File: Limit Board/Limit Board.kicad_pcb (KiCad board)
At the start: 2 copper layers, 4 parts, among them J1 Conn_01x02_Socket

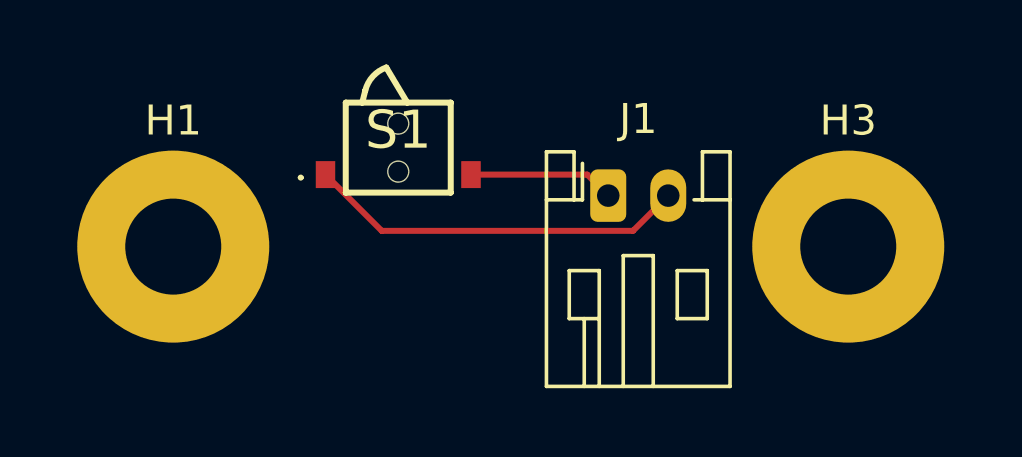
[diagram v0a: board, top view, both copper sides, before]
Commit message: Fix edge cuts
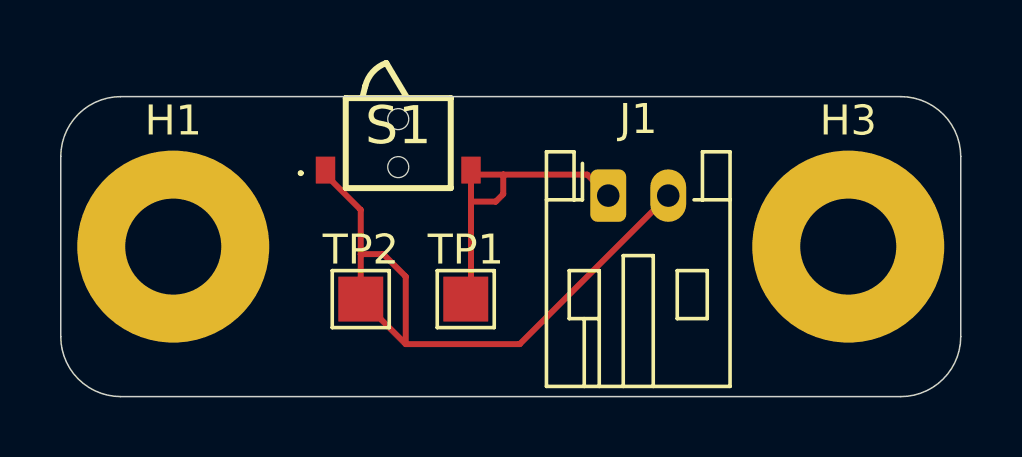
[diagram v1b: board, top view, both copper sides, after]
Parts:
- added TP1: TestPoint, TestPoint:TestPoint_Pad_1.5x1.5mm, F.Cu at (83.8, 89.2)
- added TP2: TestPoint, TestPoint:TestPoint_Pad_1.5x1.5mm, F.Cu at (80.2, 89.2)
- moved S1 0.15 mm to (81.5, 84.0)
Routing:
- net Net-(J1-Pin_2): track 12.7 -> 21.6 mm
- net Net-(J1-Pin_1): track 4.86 -> 10.9 mm
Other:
- board outline added: 30 x 10 mm
